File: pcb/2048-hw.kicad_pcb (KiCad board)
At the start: 2 copper layers, 60 x 93 mm, 101 parts, among them J1 UJC-HP-3-SMT-TR, J2 Battery, J3 SWD, SW1 SW_SPDT, SW2 PUSH_A, SW3 PUSH_B, U1 STM32F303K8Tx, U2 MCP73831-2-OT, U3 AP2210N-3.3TRG1, U4 PSP_1000_JSTK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

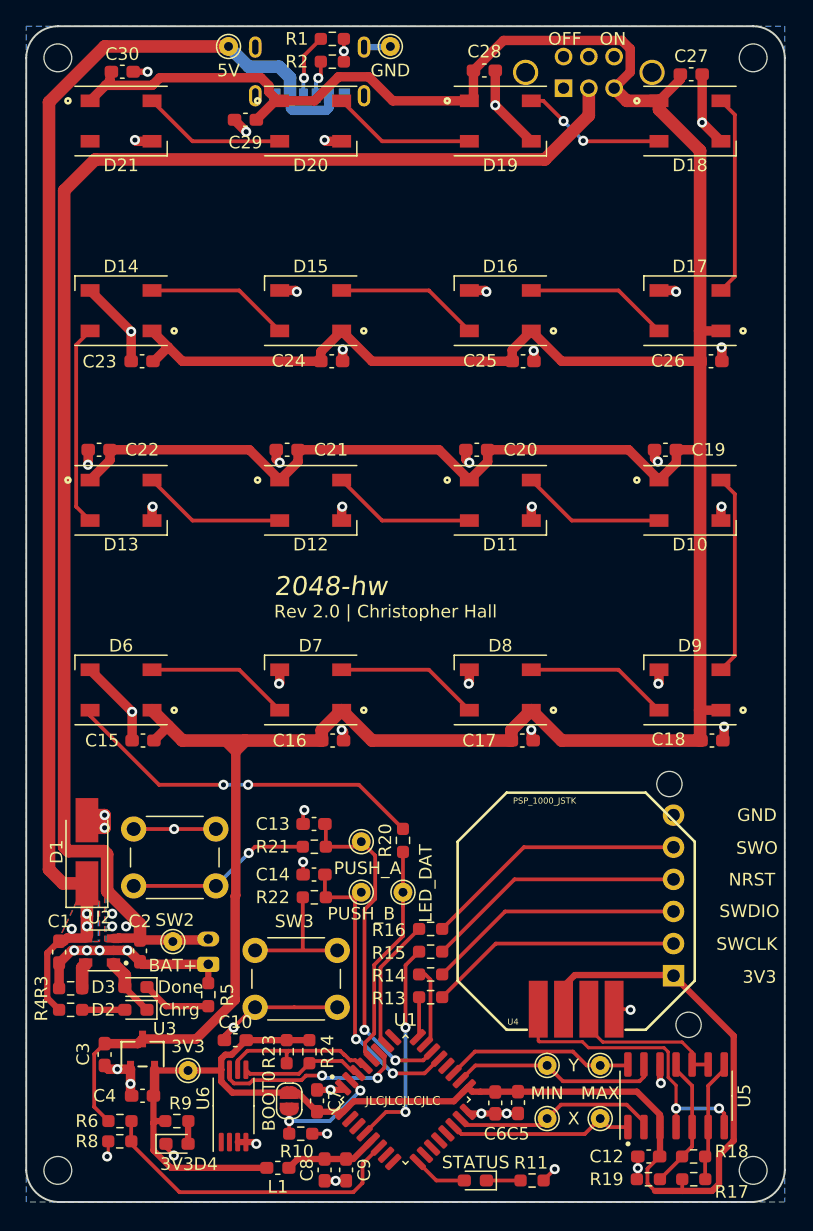
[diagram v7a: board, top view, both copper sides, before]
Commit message: pcb: Make mounting holes M3/general tidy
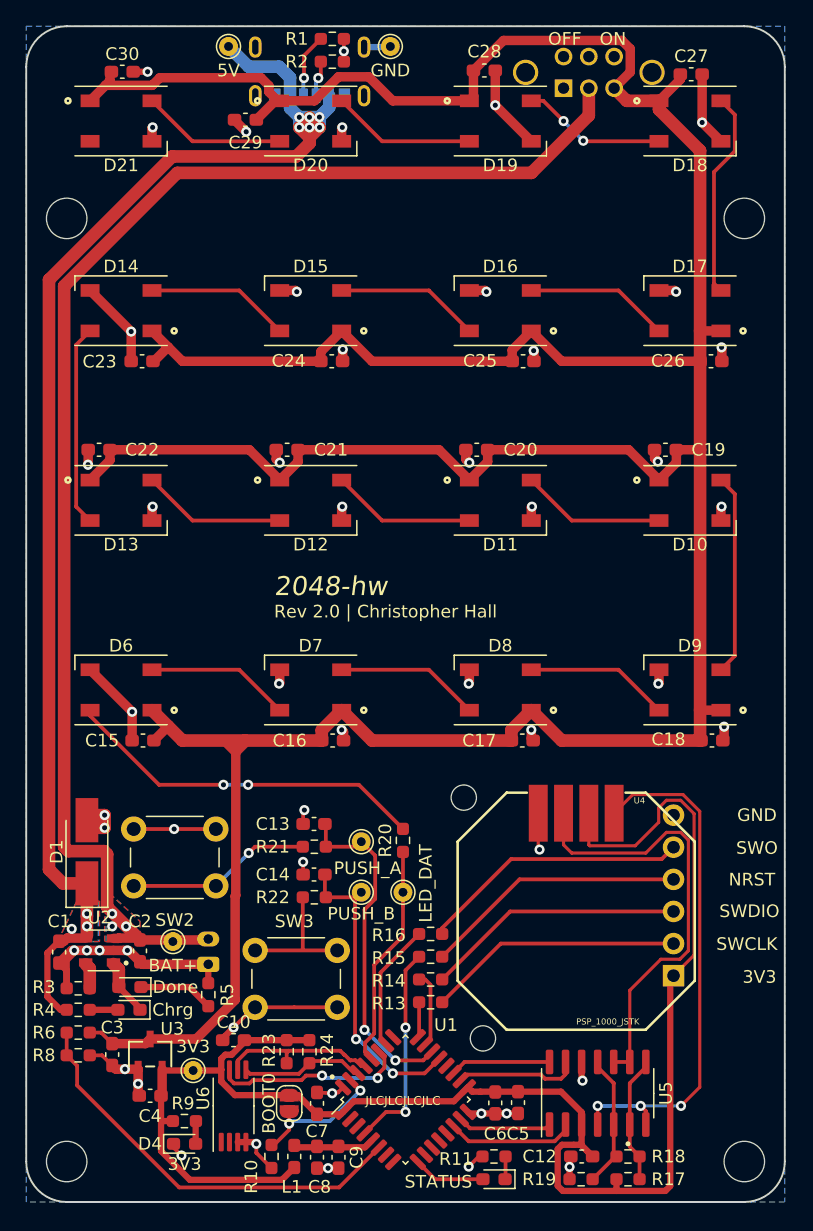
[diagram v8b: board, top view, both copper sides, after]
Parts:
- removed TP5: X_MIN, TestPoint:TestPoint_THTPad_D1.5mm_Drill0.7mm
- removed TP6: X_MAX, TestPoint:TestPoint_THTPad_D1.5mm_Drill0.7mm
- removed TP7: Y_MIN, TestPoint:TestPoint_THTPad_D1.5mm_Drill0.7mm
- removed TP8: Y_MAX, TestPoint:TestPoint_THTPad_D1.5mm_Drill0.7mm
- H1, H2, H3, H4: footprint MountingHole:MountingHole_2.2mm_M2 -> MountingHole:MountingHole_3.2mm_M3
- moved H1 12.7 mm to (123.2, 75.2)
- moved H3 12.7 mm to (176.8, 75.2)
- moved R6 7.74 mm to (124.1, 139.6), turned to 0 degrees
- moved R8 7.55 mm to (124.1, 141.4), turned to 180 degrees
- moved U5 6.20 mm to (165.2, 144.4)
- moved R19 5.33 mm to (163.9, 151.2)
- moved C12 5.30 mm to (163.9, 149.4)
- moved R17 5.20 mm to (167.6, 151.2)
- moved R18 5.19 mm to (167.6, 149.4)
- moved R11 3.56 mm to (157.0, 149.4), turned to 0 degrees
- moved R10 2.93 mm to (139.4, 149.4), turned to 90 degrees
- moved L1 1.58 mm to (141.2, 149.4), turned to 90 degrees
- moved D5 1.48 mm to (157.0, 151.2)
- moved C9 1.17 mm to (144.7, 149.5)
- moved C8 1.17 mm to (143.0, 149.5)
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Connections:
- U1 pad 18: Y_MIN -> Y_MAX
- U1 pad 19: Y_MAX -> Y_MIN
- U5 pad 1: X_MAX -> X_MIN
- U5 pad 13: Y_MIN -> Y_MAX
- U5 pad 14: Y_MAX -> Y_MIN
- U5 pad 2: X_MIN -> X_MAX
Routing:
- net JSTK_Y: track 12.7 -> 35.9 mm
- net +3V3: track 111.9 -> 129.2 mm
- net JSTK_X: track 24.4 -> 41.6 mm, vias 2 -> 3
- net +5V: track 105.2 -> 117.1 mm, vias 3 -> 9
- net X_MIN: track 16.3 -> 7.45 mm
- net Y_MIN: track 16.6 -> 7.95 mm
- net GND: track 120.7 -> 128.9 mm, vias 53 -> 51
- net BAT_ADC: track 25.3 -> 33.0 mm
- net V_BAT: track 319.0 -> 313.6 mm
- net Y_MAX: track 15.0 -> 9.73 mm
- net X_MAX: track 14.8 -> 10.2 mm
- net V_BAT_IN: track 117.1 -> 112.7 mm
- net Net-(R3-Pad1): track 2.01 -> 4.22 mm
- net BOOT0: track 9.73 -> 11.3 mm
- net LED_STATUS: track 4.29 -> 5.72 mm
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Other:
- outline, holes or cut-outs redrawn
- board text removed: "MAX"
- board text removed: "MIN"
- board text removed: "X"
- board text removed: "Y"
